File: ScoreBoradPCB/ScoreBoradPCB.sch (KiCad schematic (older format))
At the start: 128 parts, among them J1 Conn_01x08_Male, J10 Conn_01x02_Male, J2 Conn_01x08_Male, J3 Conn_01x08_Male, J4 Conn_01x04_Male, J5 Conn_01x04_Male, J6 Conn_01x02_Male, J7 Conn_01x02_Male, J8 Conn_01x06_Male, J9 Conn_01x02_Male, Q1 2N7002K, Q10 NP52N06SLG, Q11 2N7002K, Q12 NP52N06SLG, Q13 2N7002K, Q14 NP52N06SLG, Q15 BSS84, Q16 NP52N06SLG, Q17 2N7002K, Q18 BSS84, Q19 NP52N06SLG, Q2 NP52N06SLG, Q20 2N7002K, Q21 BSS84, Q22 NP52N06SLG, Q23 2N7002K, Q24 2N7002K, Q3 2N7002K, Q4 NP52N06SLG, Q5 2N7002K, Q6 NP52N06SLG, Q7 2N7002K, Q8 NP52N06SLG, Q9 2N7002K, SW1 SW_Push, SW2 SW_Push, SW3 SW_Push, SW4 SW_Push, SW5 SW_Push, SW6 SW_Push, SW7 SW_Push, U1 PIC16F1938, U2 TLP291, U3 IR2104, U4 TLP291, U5 IR2104, U6 TLP291, U7 IR2104

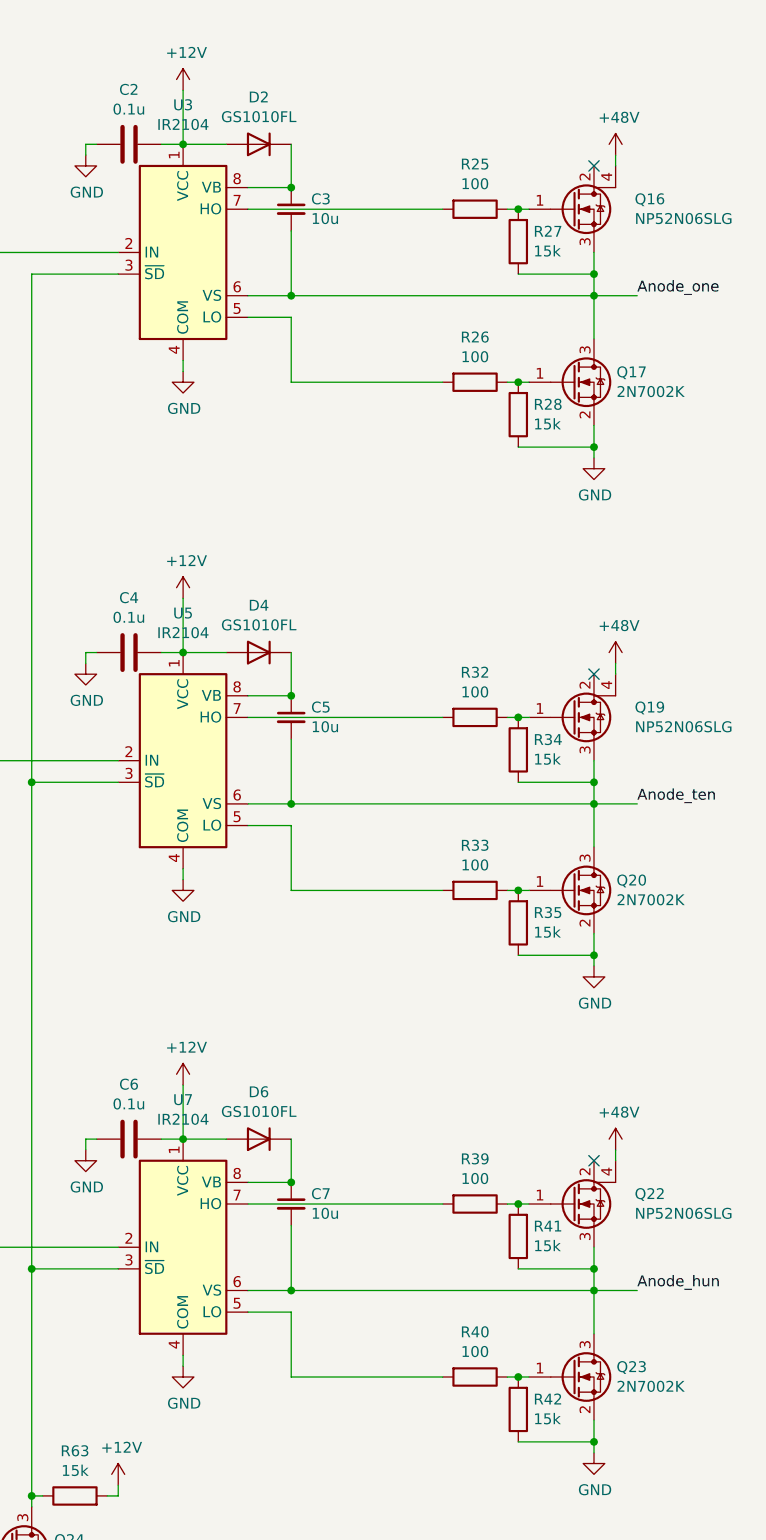
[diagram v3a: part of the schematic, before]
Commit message: ゲート抵抗を削除
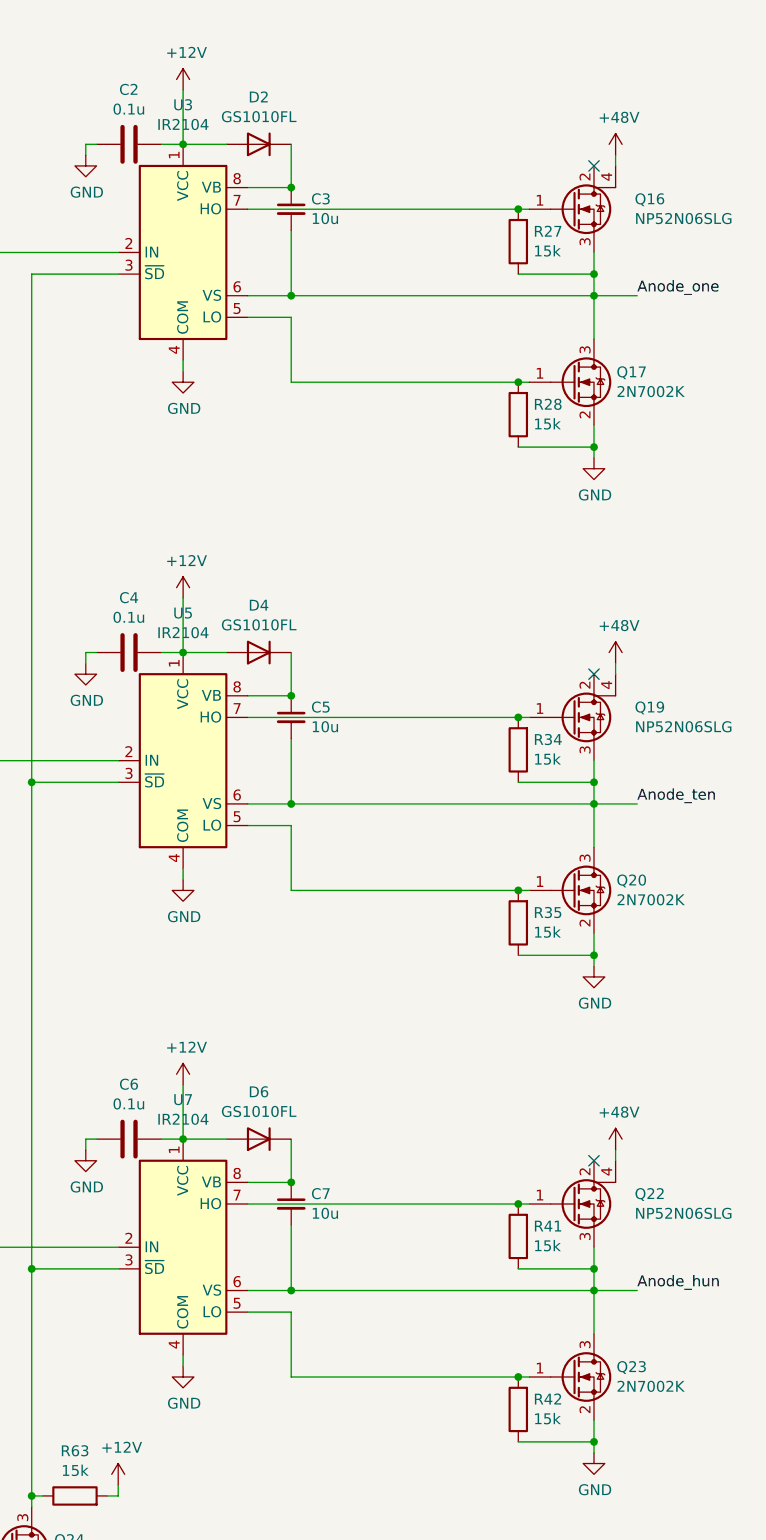
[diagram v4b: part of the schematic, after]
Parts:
- removed R25, R26, R32, R33, R39, R40: 100, Resistor_SMD:R_0603_1608Metric, symbol Device:R
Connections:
- net at U3.5 (LO): now also Q17.1 (G), R28.2
- net at U3.7 (HO): now also Q16.1 (G), R27.2
- net at U5.5 (LO): now also Q20.1 (G), R35.2
- net at U5.7 (HO): now also Q19.1 (G), R34.2
- net at U7.5 (LO): now also Q23.1 (G), R42.2
- net at U7.7 (HO): now also Q22.1 (G), R41.2
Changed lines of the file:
@@
 	8800 4400 8600 4400
-$Comp
-L Device:R R26
-U 1 1 5F65B2F2
-P 9650 4800
-F 0 "R26" V 9443 4800 50  0000 C CNN
-F 1 "100" V 9534 4800 50  0000 C CNN
-F 2 "Resistor_SMD:R_0603_1608Metric" V 9580 4800 50  0001 C CNN
-F 3 "~" H 9650 4800 50  0001 C CNN
-	1    9650 4800
-	0    1    1    0
-$EndComp
-$Comp
-L Device:R R25
-U 1 1 5F65AE60
-P 9650 4000
-F 0 "R25" V 9443 4000 50  0000 C CNN
-F 1 "100" V 9534 4000 50  0000 C CNN
-F 2 "Resistor_SMD:R_0603_1608Metric" V 9580 4000 50  0001 C CNN
-F 3 "~" H 9650 4000 50  0001 C CNN
-	1    9650 4000
-	0    1    1    0
-$EndComp
-Wire Wire Line
-	9500 4000 8600 4000
 $Comp
 L Device:Q_NMOS_GDSD Q16
@@
 Connection ~ 8800 4400
 Wire Wire Line
-	9500 4800 8800 4800
-Wire Wire Line
 	8800 4800 8800 4500
 Wire Wire Line
 	8800 4500 8600 4500
-Wire Wire Line
-	9800 4800 9850 4800
-Wire Wire Line
-	9800 4000 9850 4000
 $Comp
 L Device:R R27
@@
 	8800 6750 8600 6750
 $Comp
-L Device:R R33
-U 1 1 5F75AA9A
-P 9650 7150
-F 0 "R33" V 9443 7150 50  0000 C CNN
-F 1 "100" V 9534 7150 50  0000 C CNN
-F 2 "Resistor_SMD:R_0603_1608Metric" V 9580 7150 50  0001 C CNN
-F 3 "~" H 9650 7150 50  0001 C CNN
-	1    9650 7150
-	0    1    1    0
-$EndComp
-$Comp
-L Device:R R32
-U 1 1 5F75AAA0
-P 9650 6350
-F 0 "R32" V 9443 6350 50  0000 C CNN
-F 1 "100" V 9534 6350 50  0000 C CNN
-F 2 "Resistor_SMD:R_0603_1608Metric" V 9580 6350 50  0001 C CNN
-F 3 "~" H 9650 6350 50  0001 C CNN
-	1    9650 6350
-	0    1    1    0
-$EndComp
-Wire Wire Line
-	9500 6350 8600 6350
-$Comp
 L Device:Q_NMOS_GDSD Q19
 U 1 1 5F75AAA7
@@
 Connection ~ 8800 6750
 Wire Wire Line
-	9500 7150 8800 7150
-Wire Wire Line
 	8800 7150 8800 6850
 Wire Wire Line
 	8800 6850 8600 6850
-Wire Wire Line
-	9800 7150 9850 7150
-Wire Wire Line
-	9800 6350 9850 6350
 $Comp
 L Device:R R34
@@
 	8800 9000 8600 9000
 $Comp
-L Device:R R40
-U 1 1 5F77DE21
-P 9650 9400
-F 0 "R40" V 9443 9400 50  0000 C CNN
-F 1 "100" V 9534 9400 50  0000 C CNN
-F 2 "Resistor_SMD:R_0603_1608Metric" V 9580 9400 50  0001 C CNN
-F 3 "~" H 9650 9400 50  0001 C CNN
-	1    9650 9400
-	0    1    1    0
-$EndComp
-$Comp
-L Device:R R39
-U 1 1 5F77DE27
-P 9650 8600
-F 0 "R39" V 9443 8600 50  0000 C CNN
-F 1 "100" V 9534 8600 50  0000 C CNN
-F 2 "Resistor_SMD:R_0603_1608Metric" V 9580 8600 50  0001 C CNN
-F 3 "~" H 9650 8600 50  0001 C CNN
-	1    9650 8600
-	0    1    1    0
-$EndComp
-Wire Wire Line
-	9500 8600 8600 8600
-$Comp
 L Device:Q_NMOS_GDSD Q22
 U 1 1 5F77DE2E
@@
 Connection ~ 8800 9000
 Wire Wire Line
-	9500 9400 8800 9400
-Wire Wire Line
 	8800 9400 8800 9100
 Wire Wire Line
 	8800 9100 8600 9100
-Wire Wire Line
-	9800 9400 9850 9400
-Wire Wire Line
-	9800 8600 9850 8600
 $Comp
 L Device:R R41
@@
 	2100 8650 2100 9600
 NoConn ~ 2700 4200
+Wire Wire Line
+	8800 9400 9850 9400
+Wire Wire Line
+	8600 8600 9850 8600
+Wire Wire Line
+	8800 7150 9850 7150
+Wire Wire Line
+	8600 6350 9850 6350
+Wire Wire Line
+	8800 4800 9850 4800
+Wire Wire Line
+	8600 4000 9850 4000
 $EndSCHEMATC

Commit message: 回路修正
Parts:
- removed R27, R28, R34, R35, R41, R42: 15k, Resistor_SMD:R_0603_1608Metric, symbol Device:R
- removed R44, R45, R60, R61: 1k, Resistor_SMD:R_0603_1608Metric, symbol Device:R
- C1: value 0.1u -> 10u
- C3, C5, C7: value 10u -> 0.1u
- R43: value 1k -> 15k
- R46, R47, R48, R49: value 300 -> 1.2k
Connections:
- net at D7.2 (A): now also R43.2
